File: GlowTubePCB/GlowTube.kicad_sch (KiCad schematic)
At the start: 39 parts, among them J1 Conn_01x07, P1 Solder_Pad, P2 Solder_Pad, P3 Solder_Pad, P4 Solder_Pad, P5 Solder_Pad, P6 Solder_Pad, SW1 TS-1185EC-C-D-B, SW2 TS-1185EC-C-D-B, U1 SN74LVC2T45DCUR, U2 ESP32-WROOM-32E, U3 CP2102-GMR, U4 BL1117-33CX, U5 UMH3N, U6 MSM261D4030H1CPM

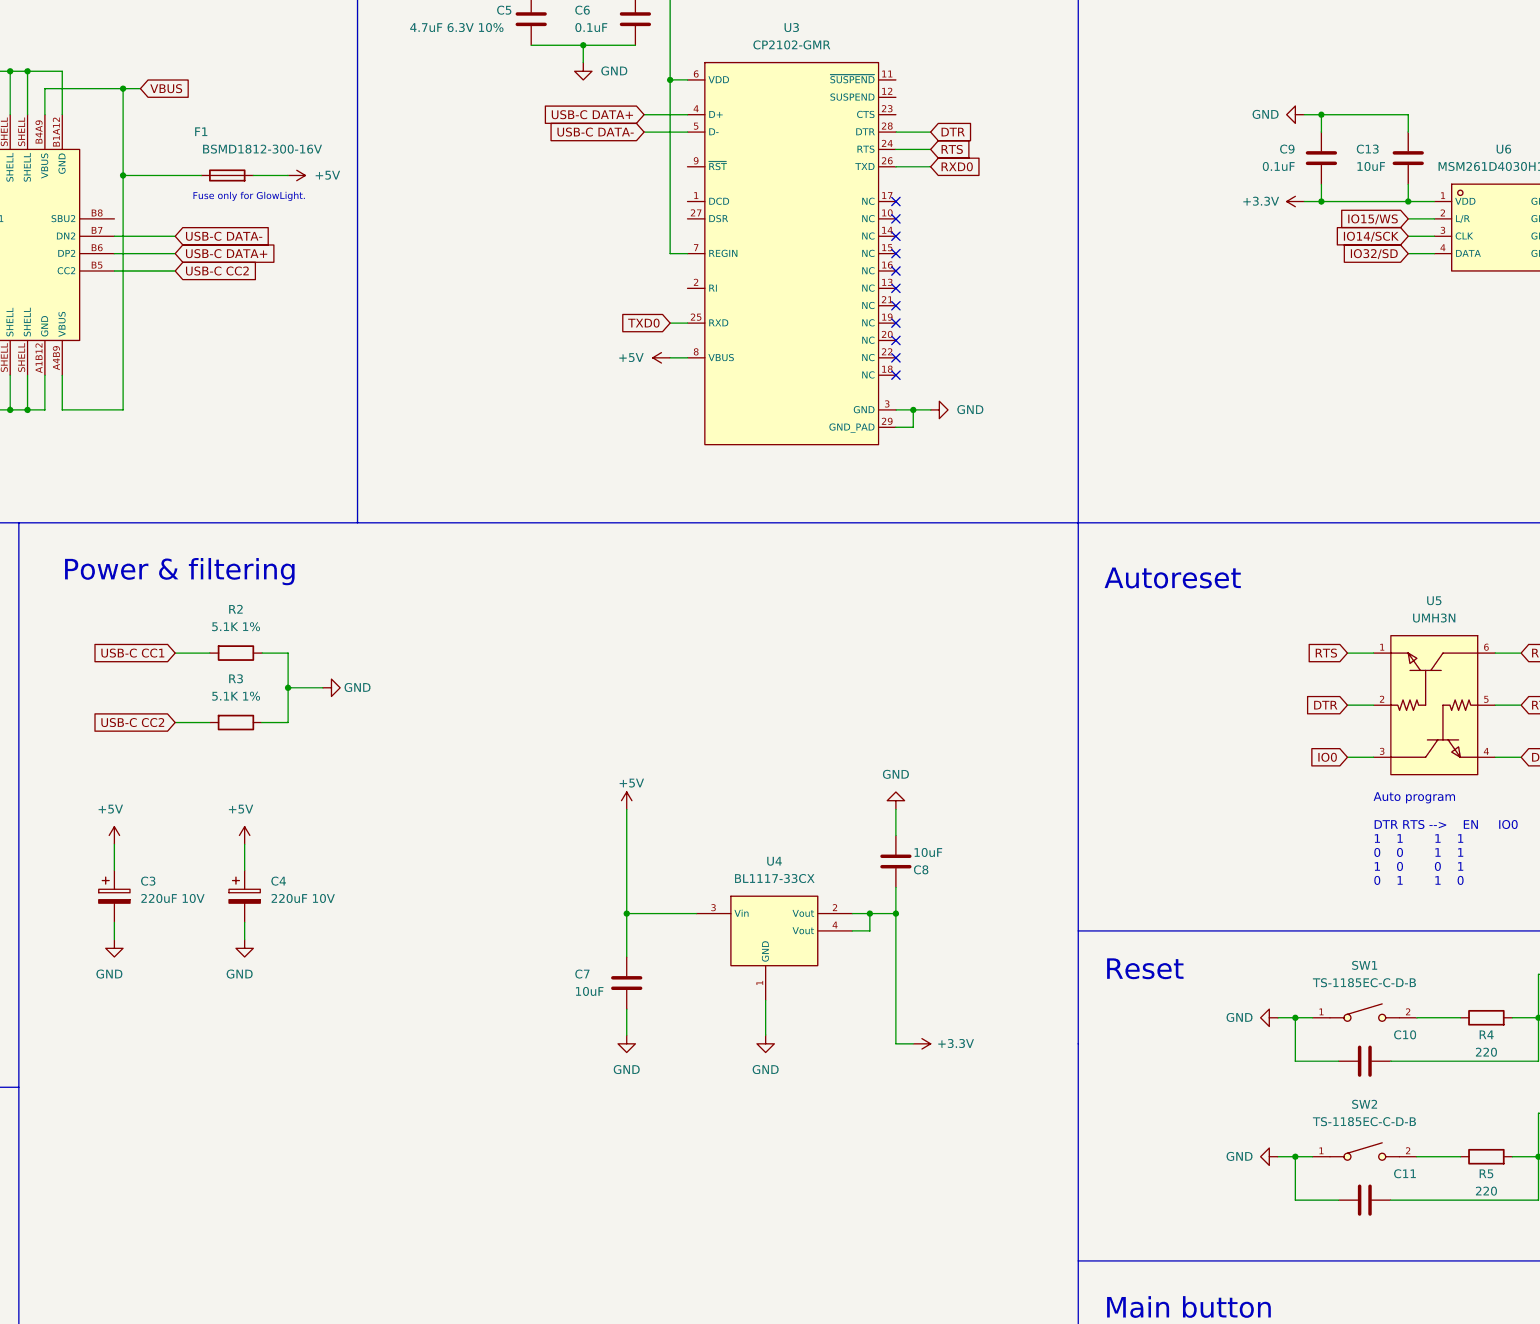
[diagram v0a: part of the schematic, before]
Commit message: added schottky diode to protect usb-c port
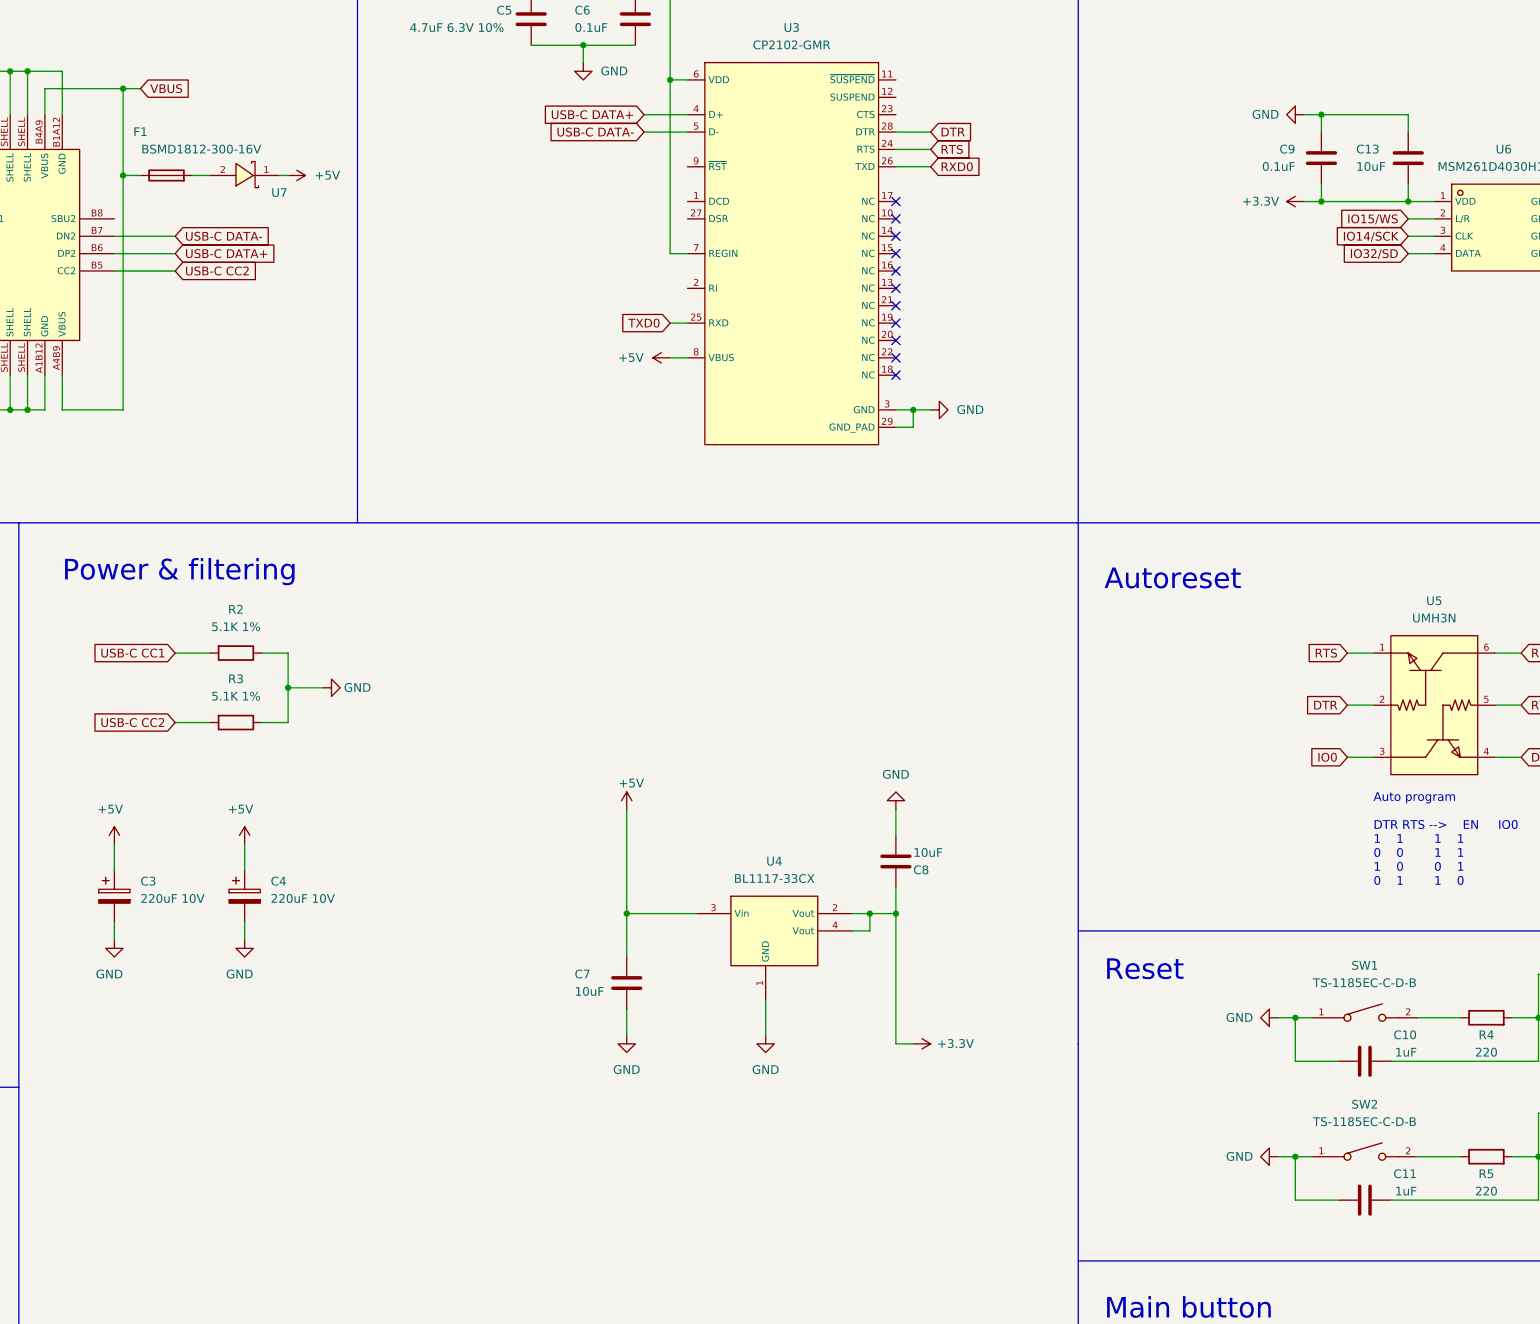
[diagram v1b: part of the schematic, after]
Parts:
- added U7: (no value), symbol MyParts:SS54
- C10, C11: value (none) -> 1uF; footprint (none) -> Capacitor_SMD:C_0603_1608Metric_Pad1.08x0.95mm_HandSolder
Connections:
- net +5V: now also U7.1 (K); no longer F1.2
- new net: F1.2, U7.2 (A)
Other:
- note removed: "Fuse only for GlowLight."
- moved on the sheet: F1
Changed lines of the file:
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@@
+    (stroke (width 0) (type default) (color 0 0 0 0))
+  )
+  (wire (pts (xy 182.88 60.96) (xy 184.15 60.96))
     (stroke (width 0) (type default) (color 0 0 0 0))
   )
@@
     (stroke (width 0) (type default) (color 0 0 0 0))
   )
-  (wire (pts (xy 179.07 60.96) (xy 184.15 60.96))
-    (stroke (width 0) (type default) (color 0 0 0 0))
-  )
   (wire (pts (xy 273.05 168.91) (xy 273.05 165.1))
     (stroke (width 0) (type default) (color 0 0 0 0))
@@
     (stroke (width 0) (type default) (color 0 0 0 0))
   )
-  (wire (pts (xy 171.45 60.96) (xy 160.02 60.96))
+  (wire (pts (xy 162.56 60.96) (xy 160.02 60.96))
     (stroke (width 0) (type default) (color 0 0 0 0))
   )
@@
   )
   (wire (pts (xy 83.82 83.82) (xy 81.28 83.82))
+    (stroke (width 0) (type default) (color 0 0 0 0))
+  )
+  (wire (pts (xy 170.18 60.96) (xy 172.72 60.96))
     (stroke (width 0) (type default) (color 0 0 0 0))
   )
@@
   (text "Pins" (at 16.51 205.74 0)
     (effects (font (size 3 3)) (justify left bottom))
-  )
-  (text "Fuse only for GlowLight." (at 170.18 64.77 0)
-    (effects (font (size 1 1)) (justify left bottom))
   )
   (text "USB-C port" (at 113.03 20.32 0)
@@
       (effects (font (size 1.27 1.27)) (justify right))
     )
-    (property "Value" "" (id 1) (at 349.25 209.55 90)
+    (property "Value" "1uF" (id 1) (at 349.25 209.55 90)
       (effects (font (size 1.27 1.27)) (justify right))
     )
-    (property "Footprint" "" (id 2) (at 309.88 210.82 0)
+    (property "Footprint" "Capacitor_SMD:C_0603_1608Metric_Pad1.08x0.95mm_HandSolder" (id 2) (at 309.88 210.82 0)
       (effects (font (size 1.27 1.27)) hide)
     )
@@
     (pin "1")
   )
+  (symbol (lib_id "MyParts:SS54") (at 177.8 60.96 180) (unit 1)
+    (in_bom yes) (on_board yes)
+    (property "Reference" "U7" (id 0) (at 182.88 63.5 0))
+    (property "Value" "" (id 1) (at 182.88 66.04 0))
+    (property "Footprint" "" (id 2) (at 177.8 63.5 0)
+      (effects (font (size 1.27 1.27) italic) hide)
+    )
+    (property "Datasheet" "https://so.szlcsc.com/global.html?c=&k=C50840" (id 3) (at 181.356 68.707 0)
+      (effects (font (size 1.27 1.27)) (justify left) hide)
+    )
+    (property "LCSC #" "C123946" (id 4) (at 179.07 68.58 0)
+      (effects (font (size 1.27 1.27)) hide)
+    )
+    (pin "1")
+    (pin "2")
+  )
   (symbol (lib_id "MyParts:BL1117-33CX") (at 255.27 160.02 0) (unit 1)
     (in_bom yes) (on_board yes) (fields_autoplaced)
@@
     (pin "1")
   )
-  (symbol (lib_id "Device:Fuse") (at 175.26 60.96 90) (unit 1)
-    (in_bom yes) (on_board yes)
-    (property "Reference" "F1" (id 0) (at 171.45 54.61 90))
-    (property "Value" "BSMD1812-300-16V" (id 1) (at 180.34 57.15 90))
-    (property "Footprint" "Fuse:Fuse_1812_4532Metric_Pad1.30x3.40mm_HandSolder" (id 2) (at 175.26 62.738 90)
-      (effects (font (size 1.27 1.27)) hide)
-    )
-    (property "Datasheet" "~" (id 3) (at 175.26 60.96 0)
-      (effects (font (size 1.27 1.27)) hide)
-    )
-    (property "LCSC #" "C883162" (id 4) (at 175.26 60.96 90)
+  (symbol (lib_id "Device:Fuse") (at 166.37 60.96 90) (unit 1)
+    (in_bom yes) (on_board yes)
+    (property "Reference" "F1" (id 0) (at 162.56 54.61 90))
+    (property "Value" "BSMD1812-300-16V" (id 1) (at 171.45 57.15 90))
+    (property "Footprint" "Fuse:Fuse_1812_4532Metric_Pad1.30x3.40mm_HandSolder" (id 2) (at 166.37 62.738 90)
+      (effects (font (size 1.27 1.27)) hide)
+    )
+    (property "Datasheet" "~" (id 3) (at 166.37 60.96 0)
+      (effects (font (size 1.27 1.27)) hide)
+    )
+    (property "LCSC #" "C883162" (id 4) (at 166.37 60.96 90)
       (effects (font (size 1.27 1.27)) hide)
     )
@@
       (effects (font (size 1.27 1.27)) (justify right))
     )
-    (property "Value" "" (id 1) (at 349.25 189.23 90)
+    (property "Value" "1uF" (id 1) (at 349.25 189.23 90)
       (effects (font (size 1.27 1.27)) (justify right))
     )
-    (property "Footprint" "" (id 2) (at 309.88 190.5 0)
+    (property "Footprint" "Capacitor_SMD:C_0603_1608Metric_Pad1.08x0.95mm_HandSolder" (id 2) (at 309.88 190.5 0)
       (effects (font (size 1.27 1.27)) hide)
     )
@@
       (reference "U6") (unit 1) (value "MSM261D4030H1CPM") (footprint "footprint:MIC-SMD_8P-L3.0-W4.0-P0.85-BL")
     )
+    (path "/33e14999-b5ae-46d2-ac28-01787a512419"
+      (reference "U7") (unit 1) (value "SS54") (footprint "footprint:SMA_L4.4-W2.8-LS5.4-RD")
+    )
     (path "/eb8d9b92-b461-41f5-9299-3a167f76d05d"

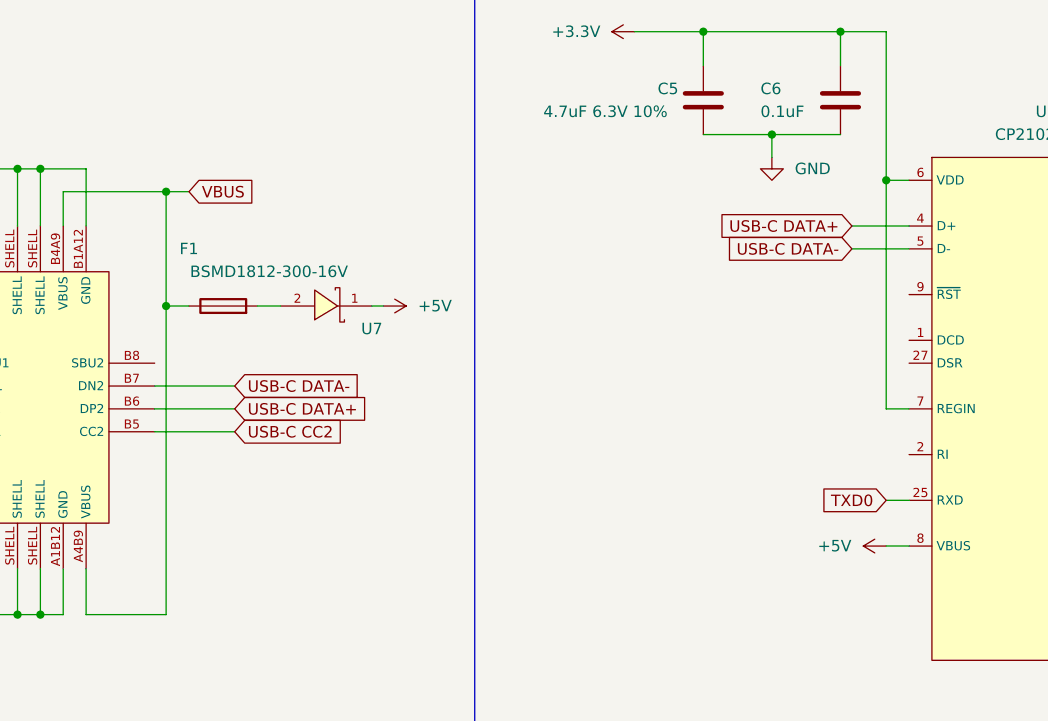
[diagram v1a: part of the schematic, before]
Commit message: added second schottky diode for less heat
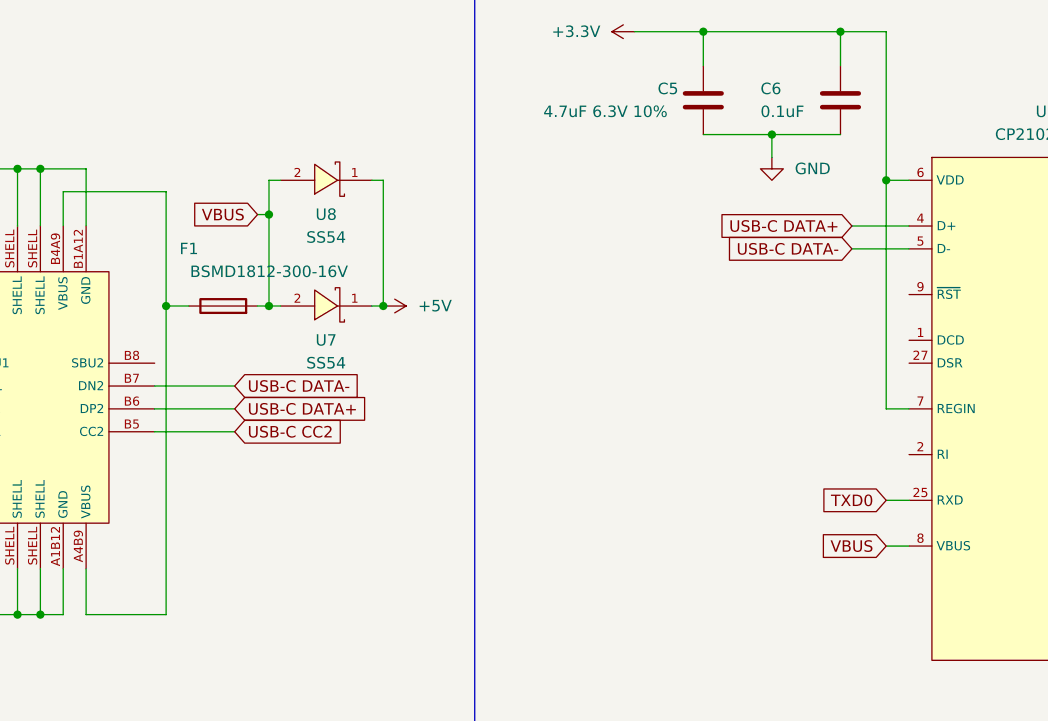
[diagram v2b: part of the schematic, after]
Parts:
- added U8: SS54, footprint:SMA_L4.4-W2.8-LS5.4-RD, symbol MyParts:SS54
- U7: value (none) -> SS54; footprint (none) -> footprint:SMA_L4.4-W2.8-LS5.4-RD
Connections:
- net +5V: now also U8.1 (K); no longer U3.8 (VBUS)
- net VBUS: now also F1.2, U3.8 (VBUS), U7.2 (A), U8.2 (A); no longer F1.1, USB1.A4B9 (VBUS), USB1.B4A9 (VBUS)
- new net: F1.1, USB1.A4B9 (VBUS), USB1.B4A9 (VBUS)
